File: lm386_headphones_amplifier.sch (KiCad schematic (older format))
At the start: 16 parts, among them J1 JACK_TRS_6PINS, J2 JACK_TRS_6PINS, P1 USB_B, U1 LM386, U2 LM386

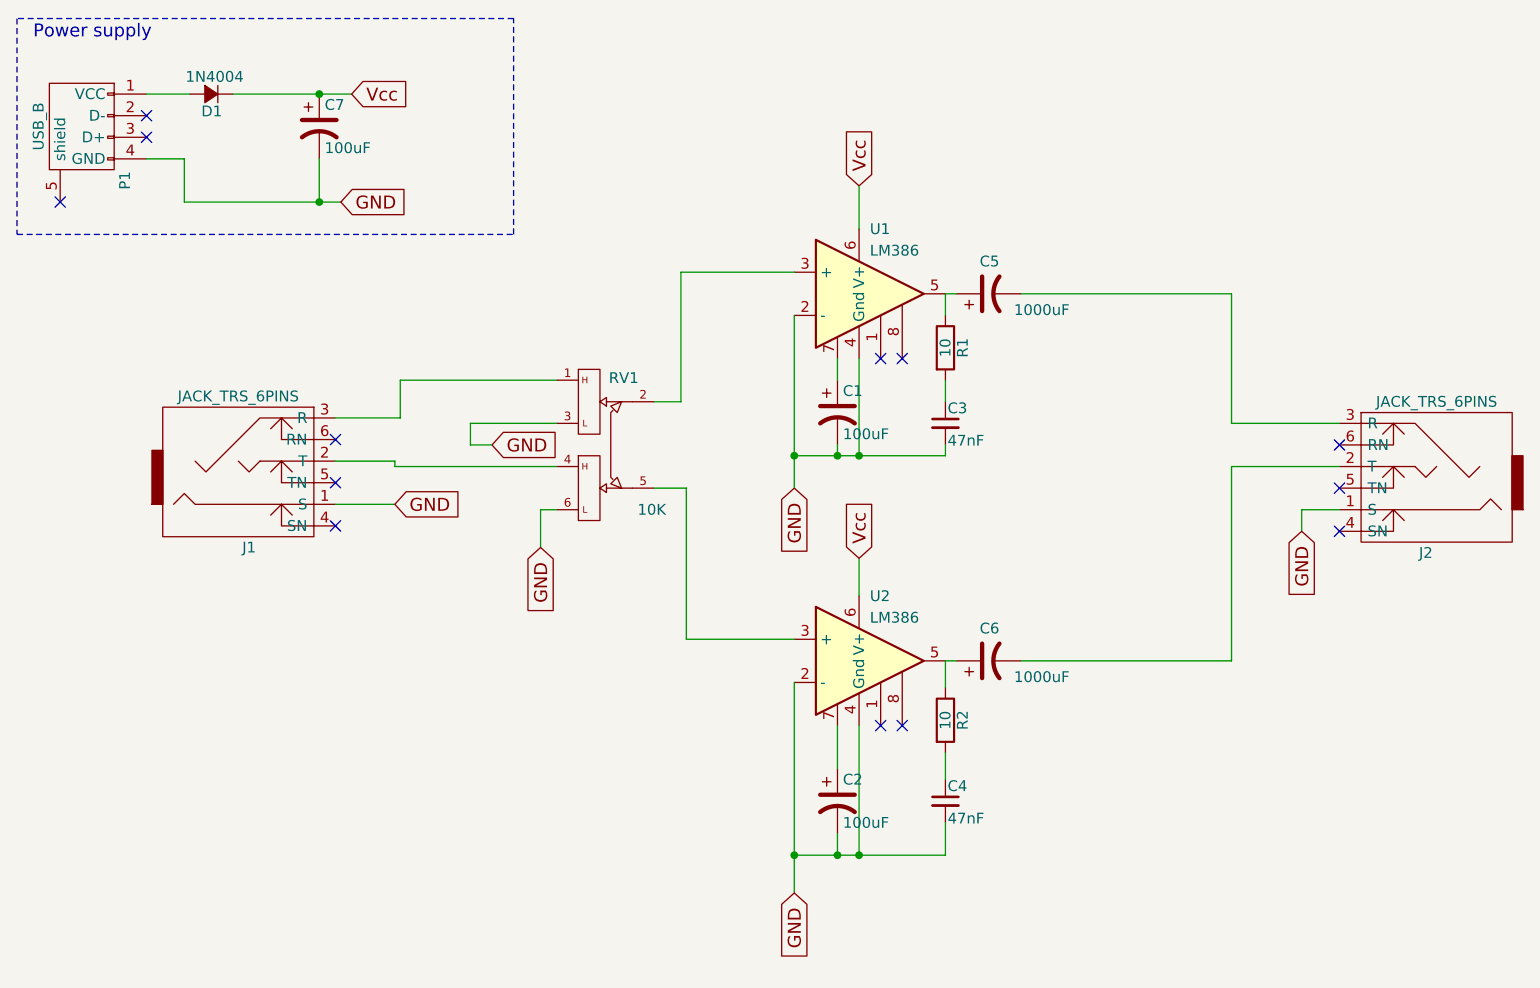
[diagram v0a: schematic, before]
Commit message: add 100 nF input jack capacitors. Wire the components in pcbnew
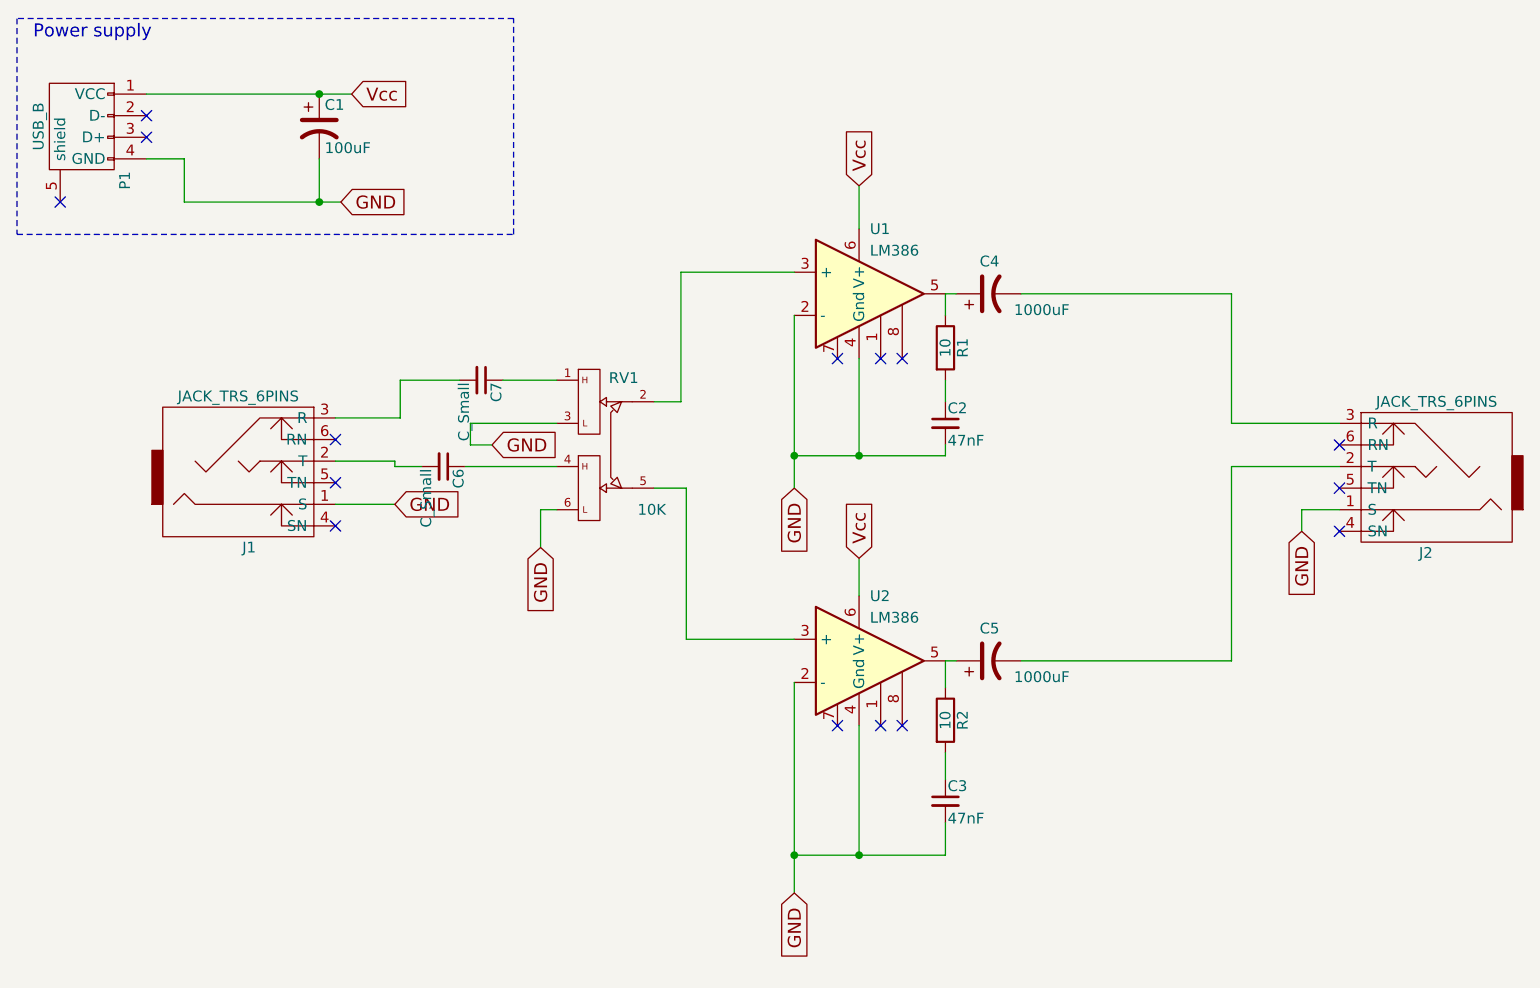
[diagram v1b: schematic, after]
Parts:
- removed C1, C2: 100uF, Capacitors_ThroughHole:C_Radial_D5_L11_P2, symbol CP1
- removed D1: 1N4004, Diodes_ThroughHole:Diode_DO-35_SOD27_Horizontal_RM10, symbol D_Small
- added C6, C7: C_Small, Capacitors_ThroughHole:C_Disc_D3_P2.5, symbol C_Small
- renumbered C7 to C1, C3 to C2, C4 to C3, C5 to C4, C6 to C5
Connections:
- net Vcc: now also P1.1 (VCC)
- net at RV1.1: now also C7.1; no longer J1.3 (R)
- net at RV1.4: now also C6.1; no longer J1.2 (T)
- new net: C6.2, J1.2 (T)
- new net: C7.2, J1.3 (R)
- no-connect marks 13 -> 15
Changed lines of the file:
@@
 Vcc
 $Comp
-L CP1 C1
-U 1 1 5AD1E1CD
-P 4600 2450
-F 0 "C1" H 4625 2550 50  0000 L CNN
-F 1 "100uF" H 4625 2350 50  0000 L CNN
-F 2 "Capacitors_ThroughHole:C_Radial_D5_L11_P2" H 4600 2450 50  0001 C CNN
-F 3 "" H 4600 2450 50  0000 C CNN
-	1    4600 2450
-	1    0    0    -1
-$EndComp
-$Comp
-L CP1 C2
-U 1 1 5AD1E3E5
-P 4600 4250
-F 0 "C2" H 4625 4350 50  0000 L CNN
-F 1 "100uF" H 4625 4150 50  0000 L CNN
-F 2 "Capacitors_ThroughHole:C_Radial_D5_L11_P2" H 4600 4250 50  0001 C CNN
-F 3 "" H 4600 4250 50  0000 C CNN
-	1    4600 4250
-	1    0    0    -1
-$EndComp
-$Comp
-L CP1 C5
+L CP1 C4
 U 1 1 5AD1E933
 P 5300 1900
-F 0 "C5" V 5450 1850 50  0000 L CNN
+F 0 "C4" V 5450 1850 50  0000 L CNN
 F 1 "1000uF" V 5225 1525 50  0000 L CNN
 F 2 "Capacitors_ThroughHole:C_Radial_D10_L13_P5" H 5300 1900 50  0001 C CNN
@@
 $EndComp
 $Comp
-L CP1 C6
+L CP1 C5
 U 1 1 5AD1EA62
 P 5300 3600
-F 0 "C6" V 5450 3550 50  0000 L CNN
+F 0 "C5" V 5450 3550 50  0000 L CNN
 F 1 "1000uF" V 5225 3225 50  0000 L CNN
 F 2 "Capacitors_ThroughHole:C_Radial_D10_L13_P5" H 5300 3600 50  0001 C CNN
@@
 Text Notes 875  725  0    60   ~ 0
 Power supply
-$Comp
-L D_Small D1
-U 1 1 5AD1FE9A
-P 1700 975
-F 0 "D1" H 1650 1055 50  0000 L CNN
-F 1 "1N4004" H 1550 895 50  0000 L CNN
-F 2 "Diodes_ThroughHole:Diode_DO-35_SOD27_Horizontal_RM10" V 1700 975 50  0001 C CNN
-F 3 "" V 1700 975 50  0000 C CNN
-	1    1700 975
-	-1   0    0    1
-$EndComp
 Text GLabel 2350 975  2    60   Input ~ 0
 Vcc
 $Comp
-L CP1 C7
+L CP1 C1
 U 1 1 5AD1EE71
 P 2200 1125
-F 0 "C7" H 2225 1225 50  0000 L CNN
+F 0 "C1" H 2225 1225 50  0000 L CNN
 F 1 "100uF" H 2225 1025 50  0000 L CNN
 F 2 "Capacitors_ThroughHole:C_Radial_D5_L11_P2" H 2200 1125 50  0001 C CNN
@@
 $EndComp
 $Comp
-L C_Small C4
+L C_Small C3
 U 1 1 5AE8B25F
 P 5100 4250
-F 0 "C4" H 5110 4320 50  0000 L CNN
+F 0 "C3" H 5110 4320 50  0000 L CNN
 F 1 "47nF" H 5110 4170 50  0000 L CNN
 F 2 "Capacitors_ThroughHole:C_Disc_D3_P2.5" H 5100 4250 50  0001 C CNN
@@
 $EndComp
 $Comp
-L C_Small C3
+L C_Small C2
 U 1 1 5AE8B2E9
 P 5100 2500
-F 0 "C3" H 5110 2570 50  0000 L CNN
+F 0 "C2" H 5110 2570 50  0000 L CNN
 F 1 "47nF" H 5110 2420 50  0000 L CNN
 F 2 "Capacitors_ThroughHole:C_Disc_D3_P2.5" H 5100 2500 50  0001 C CNN
@@
 	2575 2475 2575 2300
 Wire Wire Line
-	2575 2300 3300 2300
-Wire Wire Line
-	2550 2700 3300 2700
-Wire Wire Line
 	2900 2500 3300 2500
 Wire Wire Line
@@
 Wire Wire Line
 	6425 2700 6425 3600
-Wire Wire Line
-	4600 2200 4600 2300
 Wire Wire Line
 	4400 2000 4400 2800
@@
 Wire Wire Line
 	4700 2650 4700 2200
-Connection ~ 4600 2650
 Connection ~ 4700 2650
-Wire Wire Line
-	4600 3900 4600 4100
 Wire Wire Line
 	4400 4500 5100 4500
 Connection ~ 4400 4500
-Connection ~ 4600 4500
 Connection ~ 4700 4500
 Wire Wire Line
@@
 	4400 3700 4400 4675
 Wire Wire Line
-	1400 975  1600 975
+	1400 975  2350 975
 Wire Wire Line
 	2900 2600 2900 2500
@@
 	4700 1400 4700 1600
 Wire Wire Line
-	4600 2600 4600 2650
-Wire Wire Line
-	4600 4400 4600 4500
-Wire Wire Line
 	4700 3900 4700 4500
 Wire Wire Line
@@
 Wire Wire Line
 	4700 3300 4700 3125
-Wire Wire Line
-	1800 975  2350 975
 Wire Wire Line
 	1575 1475 2300 1475
@@
 NoConn ~ 6925 2800
 NoConn ~ 6925 3000
+NoConn ~ 4600 2200
+NoConn ~ 4600 3900
+$Comp
+L C_Small C7
+U 1 1 5AEF6926
+P 2950 2300
+F 0 "C7" H 2960 2370 50  0000 L CNN
+F 1 "C_Small" H 2960 2220 50  0000 L CNN
+F 2 "Capacitors_ThroughHole:C_Disc_D3_P2.5" H 2950 2300 50  0001 C CNN
+F 3 "" H 2950 2300 50  0000 C CNN
+	1    2950 2300
+	0    1    1    0
+$EndComp
+$Comp
+L C_Small C6
+U 1 1 5AEF69B1
+P 2775 2700
+F 0 "C6" H 2785 2770 50  0000 L CNN
+F 1 "C_Small" H 2785 2620 50  0000 L CNN
+F 2 "Capacitors_ThroughHole:C_Disc_D3_P2.5" H 2775 2700 50  0001 C CNN
+F 3 "" H 2775 2700 50  0000 C CNN
+	1    2775 2700
+	0    1    1    0
+$EndComp
+Wire Wire Line
+	2575 2300 2850 2300
+Wire Wire Line
+	3050 2300 3300 2300
+Wire Wire Line
+	2550 2700 2675 2700
+Wire Wire Line
+	2875 2700 3300 2700
 $EndSCHEMATC

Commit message: use large usb type b connector. move stuff around a bit
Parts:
- P1: footprint Connect:USB_Micro-B -> Connect:USB_B
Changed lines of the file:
@@
 F 0 "P1" H 1300 975 50  0000 C CNN
 F 1 "USB_B" H 1050 1375 50  0000 C CNN
-F 2 "Connect:USB_Micro-B" V 1050 1075 50  0001 C CNN
+F 2 "Connect:USB_B" V 1050 1075 50  0001 C CNN
 F 3 "" V 1050 1075 50  0000 C CNN
 	1    1100 1175
